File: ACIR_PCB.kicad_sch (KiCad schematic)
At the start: 32 parts, among them J1 TestPoint, J10 TestPoint, J11 TestPoint, J12 TestPoint, J13 TestPoint, J14 TestPoint, J15 TestPoint, J2 TestPoint, J3 TestPoint, J4 TestPoint, J5 TestPoint, J6 TestPoint, J7 TestPoint, J8 TestPoint, J9 TestPoint

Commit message: Align 1S 4P test points horizontally, add Cell 4 test points (J16, J17), and connect pack test points
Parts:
- added J16, J17: TestPoint, TestPoint:TestPoint_Bridge_Pitch2.54mm_Drill1.3mm, symbol Connector:Conn_01x01_Pin
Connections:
- net 4P_B+: now also J16.1 (Pin_1)
- net 4P_B-: now also J17.1 (Pin_1)
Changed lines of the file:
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@@
 		)
 	)
-	(sheet_instances
+		(symbol
+		(lib_id "Connector:Conn_01x01_Pin")
+		(at 110.49 21.59 270)
+		(unit 1)
+		(body_style 1)
+		(exclude_from_sim no)
+		(in_bom yes)
+		(on_board yes)
+		(in_pos_files yes)
+		(dnp no)
+		(fields_autoplaced yes)
+		(property "Reference" "J16"
+			(at 125.73 20.9549 90)
+			(show_name no)
+			(do_not_autoplace no)
+			(effects
+				(font
+					(size 1.27 1.27)
+				)
+				(justify left)
+			)
+		)
+		(property "Value" "TestPoint"
+			(at 125.73 23.4949 90)
+			(show_name no)
+			(do_not_autoplace no)
+			(effects
+				(font
+					(size 1.27 1.27)
+				)
+				(justify left)
+			)
+		)
+		(property "Footprint" "TestPoint:TestPoint_Bridge_Pitch2.54mm_Drill1.3mm"
+			(at 124.46 21.59 0)
+			(hide yes)
+			(show_name no)
+			(do_not_autoplace no)
+			(effects
+				(font
+					(size 1.27 1.27)
+				)
+			)
+		)
+		(property "Datasheet" ""
+			(at 124.46 21.59 0)
+			(hide yes)
+			(show_name no)
+			(do_not_autoplace no)
+			(effects
+				(font
+					(size 1.27 1.27)
+				)
+			)
+		)
+		(property "Description" ""
+			(at 124.46 21.59 0)
+			(show_name no)
+			(do_not_autoplace no)
+			(effects
+				(font
+					(size 1.27 1.27)
+				)
+			)
+		)
+		(property "Sim.Device" ""
+			(at 124.46 21.59 0)
+			(hide yes)
+			(show_name no)
+			(do_not_autoplace no)
+			(effects
+				(font
+					(size 1.27 1.27)
+				)
+			)
+		)
+		(property "Sim.Pins" ""
+			(at 124.46 21.59 0)
+			(hide yes)
+			(show_name no)
+			(do_not_autoplace no)
+			(effects
+				(font
+					(size 1.27 1.27)
+				)
+			)
+		)
+		(property "Sim.Type" ""
+			(at 124.46 21.59 0)
+			(hide yes)
+			(show_name no)
+			(do_not_autoplace no)
+			(effects
+				(font
+					(size 1.27 1.27)
+				)
+			)
+		)
+		(pin "1"
+		)
+		(instances
+			(project "ACIR_PCB"
+				(path "/55445bf8-1e44-4cff-8573-6b24cd106f65"
+					(reference "J16")
+					(unit 1)
+				)
+			)
+		)
+	)
+	(symbol
+		(lib_id "Connector:Conn_01x01_Pin")
+		(at 110.49 45.72 90)
+		(unit 1)
+		(body_style 1)
+		(exclude_from_sim no)
+		(in_bom yes)
+		(on_board yes)
+		(in_pos_files yes)
+		(dnp no)
+		(fields_autoplaced yes)
+		(property "Reference" "J17"
+			(at 125.73 43.8149 90)
+			(show_name no)
+			(do_not_autoplace no)
+			(effects
+				(font
+					(size 1.27 1.27)
+				)
+				(justify right)
+			)
+		)
+		(property "Value" "TestPoint"
+			(at 125.73 46.3549 90)
+			(show_name no)
+			(do_not_autoplace no)
+			(effects
+				(font
+					(size 1.27 1.27)
+				)
+				(justify right)
+			)
+		)
+		(property "Footprint" "TestPoint:TestPoint_Bridge_Pitch2.54mm_Drill1.3mm"
+			(at 124.46 45.72 0)
+			(hide yes)
+			(show_name no)
+			(do_not_autoplace no)
+			(effects
+				(font
+					(size 1.27 1.27)
+				)
+			)
+		)
+		(property "Datasheet" ""
+			(at 124.46 45.72 0)
+			(hide yes)
+			(show_name no)
+			(do_not_autoplace no)
+			(effects
+				(font
+					(size 1.27 1.27)
+				)
+			)
+		)
+		(property "Description" ""
+			(at 124.46 45.72 0)
+			(show_name no)
+			(do_not_autoplace no)
+			(effects
+				(font
+					(size 1.27 1.27)
+				)
+			)
+		)
+		(property "Sim.Device" ""
+			(at 124.46 45.72 0)
+			(hide yes)
+			(show_name no)
+			(do_not_autoplace no)
+			(effects
+				(font
+					(size 1.27 1.27)
+				)
+			)
+		)
+		(property "Sim.Pins" ""
+			(at 124.46 45.72 0)
+			(hide yes)
+			(show_name no)
+			(do_not_autoplace no)
+			(effects
+				(font
+					(size 1.27 1.27)
+				)
+			)
+		)
+		(property "Sim.Type" ""
+			(at 124.46 45.72 0)
+			(hide yes)
+			(show_name no)
+			(do_not_autoplace no)
+			(effects
+				(font
+					(size 1.27 1.27)
+				)
+			)
+		)
+		(pin "1"
+		)
+		(instances
+			(project "ACIR_PCB"
+				(path "/55445bf8-1e44-4cff-8573-6b24cd106f65"
+					(reference "J17")
+					(unit 1)
+				)
+			)
+		)
+	)
+(sheet_instances
 		(path "/"
 			(page "1")

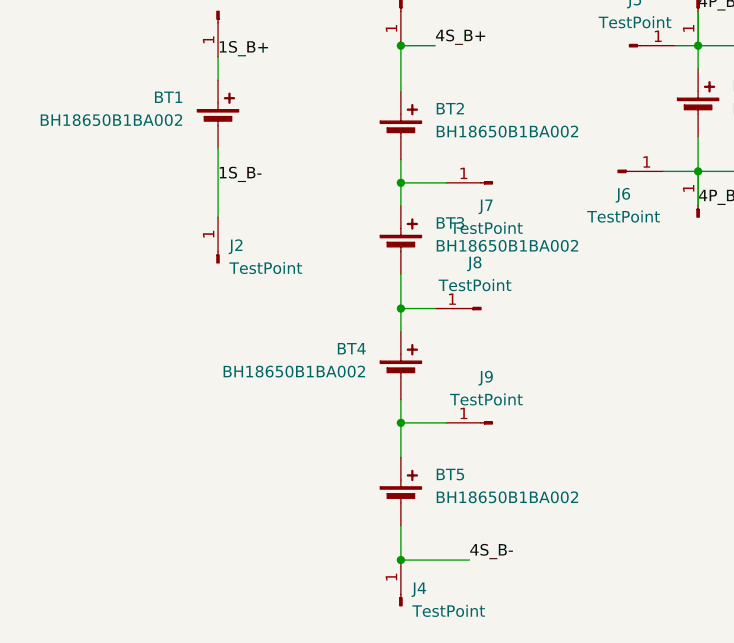
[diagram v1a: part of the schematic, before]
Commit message: Add and align dedicated test points and bare-copper circular zones for every cell in 4S1P with knockout PT Sans labels
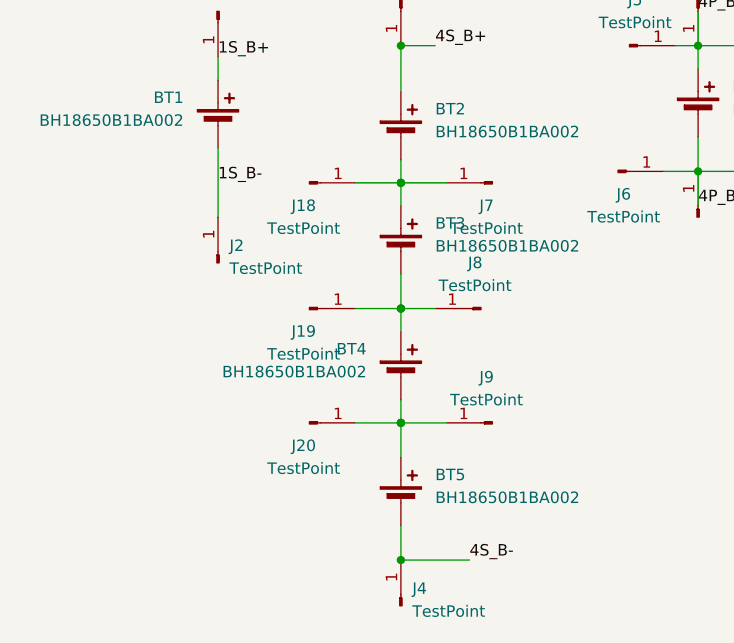
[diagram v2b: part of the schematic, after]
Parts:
- added J18, J19, J20: TestPoint, TestPoint:TestPoint_Bridge_Pitch2.54mm_Drill1.3mm, symbol Connector:Conn_01x01_Pin
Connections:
- net at BT3.2 (-), BT4.1 (+), J8.1 (Pin_1): now also J19.1 (Pin_1)
- net at BT4.2 (-), BT5.1 (+), J9.1 (Pin_1): now also J20.1 (Pin_1)
- net at BT2.2 (-), BT3.1 (+), J7.1 (Pin_1): now also J18.1 (Pin_1)
